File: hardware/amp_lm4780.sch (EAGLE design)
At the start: 77 parts, among them IC2 OPA2333D, Q1 MOSFET-NCHANNEL_SOT23-3, Q2 MOSFET-NCHANNEL_SOT23-3, T1 BC856, X1 2508-5, X2 uC

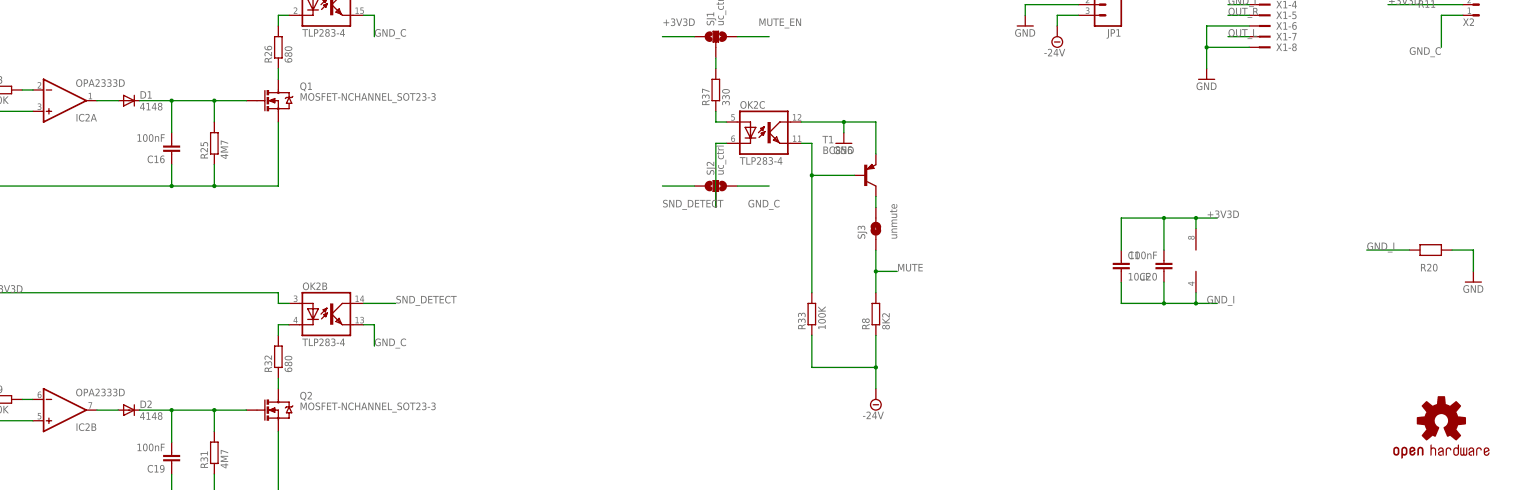
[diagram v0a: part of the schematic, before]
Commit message: fix gnd_c in amp_lm4780
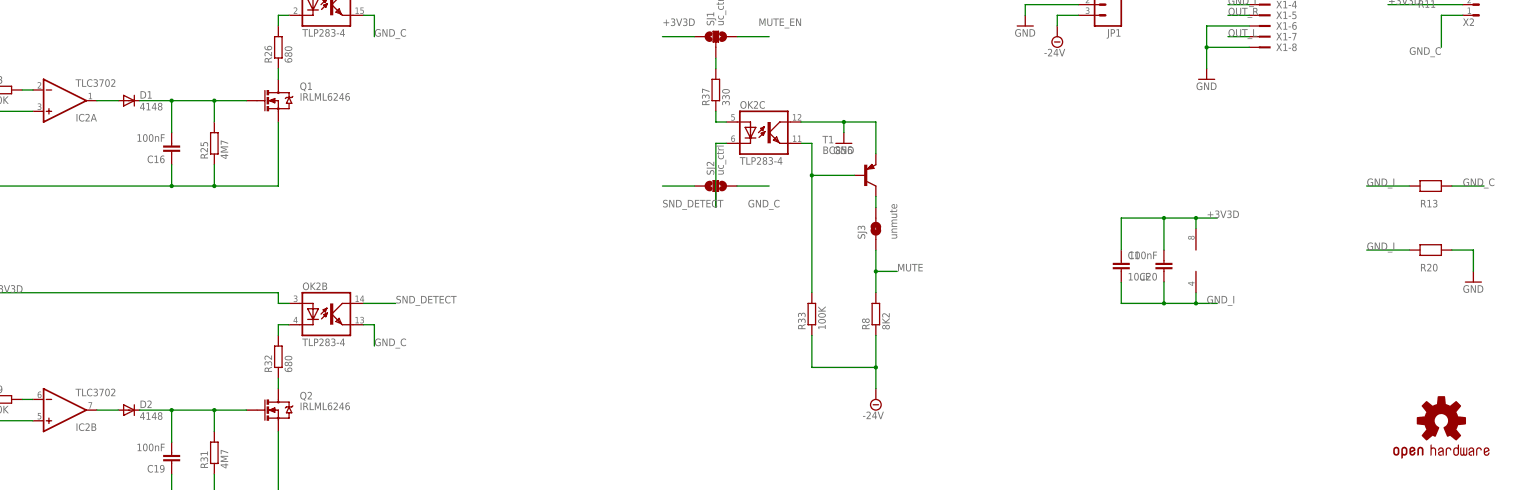
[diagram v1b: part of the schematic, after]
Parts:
- added R13: 0R_0805, Simplex-Jumpers:0R_0805
- IC2: value OPA2333D -> TLC3702
- Q1, Q2: value MOSFET-NCHANNEL_SOT23-3 -> IRLML6246
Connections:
- net N$16 renamed NONINV_IN_A
- net N$24 renamed INV_IN_A
- net N$27 renamed OUT_A
- net N$29 renamed NONINV_IN_B
- net N$32 renamed INV_IN_B
- net N$34 renamed OUTB
- net GND_C: now also R13.P$2
- net GND_I: now also R13.P$1
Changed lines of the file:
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@@
 <part name="R24" library="rcl" deviceset="R-EU_" device="R0805W" value="4M7"/>
 <part name="C15" library="rcl" deviceset="C-EU" device="C0805" value="100nF"/>
-<part name="IC2" library="linear" deviceset="OPA2333" device="D"/>
+<part name="IC2" library="linear" deviceset="OPA2333" device="D" value="TLC3702"/>
 <part name="C16" library="rcl" deviceset="C-EU" device="C0805" value="100nF"/>
 <part name="R25" library="rcl" deviceset="R-EU_" device="R0805W" value="4M7"/>
-<part name="Q1" library="Simplex-DiscreteSemi" deviceset="MOSFET-NCHANNEL" device="_SOT23-3"/>
+<part name="Q1" library="Simplex-DiscreteSemi" deviceset="MOSFET-NCHANNEL" device="_SOT23-3" value="IRLML6246"/>
 <part name="D1" library="diode" deviceset="CGRM400*-G" device="" technology="1" value="4148"/>
 <part name="R26" library="rcl" deviceset="R-EU_" device="R0805W" value="680"/>
@@
 <part name="C19" library="rcl" deviceset="C-EU" device="C0805" value="100nF"/>
 <part name="R31" library="rcl" deviceset="R-EU_" device="R0805W" value="4M7"/>
-<part name="Q2" library="Simplex-DiscreteSemi" deviceset="MOSFET-NCHANNEL" device="_SOT23-3"/>
+<part name="Q2" library="Simplex-DiscreteSemi" deviceset="MOSFET-NCHANNEL" device="_SOT23-3" value="IRLML6246"/>
 <part name="D2" library="diode" deviceset="CGRM400*-G" device="" technology="1" value="4148"/>
 <part name="R32" library="rcl" deviceset="R-EU_" device="R0805W" value="680"/>
@@
 <part name="R5" library="rcl" deviceset="R-EU_" device="R0805W" value="?K"/>
 <part name="R7" library="rcl" deviceset="R-EU_" device="R0805W" value="?K"/>
+<part name="R13" library="Simplex-Jumpers" deviceset="0R" device="_0805"/>
 </parts>
 <sheets>
@@
 <instance part="R5" gate="G$1" x="30.48" y="116.84" rot="R180"/>
 <instance part="R7" gate="G$1" x="33.02" y="43.18" rot="R180"/>
+<instance part="R13" gate="G$1" x="429.26" y="88.9"/>
 </instances>
 <busses>
@@
 <wire x1="236.22" y1="205.74" x2="236.22" y2="203.2" width="0.1524" layer="91"/>
 </segment>
-</net>
-<net name="N$16" class="0">
+<segment>
+<pinref part="R13" gate="G$1" pin="P$1"/>
+<wire x1="424.18" y1="88.9" x2="414.02" y2="88.9" width="0.1524" layer="91"/>
+<label x="414.02" y="88.9" size="1.778" layer="95"/>
+</segment>
+</net>
+<net name="NONINV_IN_A" class="0">
 <segment>
 <pinref part="C14" gate="G$1" pin="1"/>
@@
 </segment>
 </net>
-<net name="N$24" class="0">
+<net name="INV_IN_A" class="0">
 <segment>
 <pinref part="R23" gate="G$1" pin="2"/>
@@
 </segment>
 </net>
-<net name="N$27" class="0">
+<net name="OUT_A" class="0">
 <segment>
 <pinref part="IC2" gate="A" pin="OUT"/>
@@
 </segment>
 </net>
-<net name="N$29" class="0">
+<net name="NONINV_IN_B" class="0">
 <segment>
 <pinref part="C17" gate="G$1" pin="1"/>
@@
 </segment>
 </net>
-<net name="N$32" class="0">
+<net name="INV_IN_B" class="0">
 <segment>
 <pinref part="R29" gate="G$1" pin="2"/>
@@
 </segment>
 </net>
-<net name="N$34" class="0">
+<net name="OUTB" class="0">
 <segment>
 <wire x1="111.76" y1="35.56" x2="116.84" y2="35.56" width="0.1524" layer="91"/>
@@
 <label x="266.7" y="83.82" size="1.778" layer="95"/>
 </segment>
-</net>
+<segment>
+<pinref part="R13" gate="G$1" pin="P$2"/>
+<wire x1="434.34" y1="88.9" x2="441.96" y2="88.9" width="0.1524" layer="91"/>
+<label x="436.88" y="88.9" size="1.778" layer="95"/>
+</segment>
+</net>

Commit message: add buffer to snd detect circuit
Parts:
- added C27, C28, C29: 100nF, rcl:C-EUC0805
- added D3, D4, D5, D6: BZM55C3V3, diode:DIODE-MICROMELF-W
- added IC1: OPA2333, linear:OPA2333D
- added R14, R34: 4K7, rcl:R-EU_R0805W
- added R15, R41: 10K, rcl:R-EU_R0805W
- added R17, R40: 47K, rcl:R-EU_R0805W
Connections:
- new net N$11: D3.C, D4.A, IC1A.-IN, R15.1, R17.2
- new net N$12: IC1B.+IN, R34.2
- new net N$13: IC1B.OUT, R40.1, R7.2
- new net N$15: D5.C, D6.A, IC1B.-IN, R40.2, R41.1
- new net N$16: C29.1, SJ5.1
- new net N$17: C29.2, R41.2
- new net N$18: C28.2, R15.2
- new net N$19: C28.1, SJ6.1
- net +3V3D: now also C27.2, D4.C, D6.C, IC1P.V+
- net GND_I: now also C27.1, D3.A, D5.A, IC1P.V-, R14.1, R34.1
- net N$5: now also IC1A.+IN, R14.2; no longer R7.2, SJ5.1
- net N$7: now also IC1A.OUT, R17.1; no longer SJ6.1
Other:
- moved on the sheet: C1, C14, C15, C16, C17, C18, C19, D1, D2, IC2A, IC2B, OK2A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

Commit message: redesign snd_detect circuit layout
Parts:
- removed D4, D6: BZM55C3V3, diode:DIODE-MICROMELF-W
- removed R15, R41: 10K, rcl:R-EU_R0805W
- added C30, C31: 1nF, rcl:C-EUC0805
- added C32, C33: 1uF, rcl:C-EUC0805
- added C34: 10uF, rcl:C-EUC1206K
- added D7, D8: BZM55C3V3, diode:DIODE-MICROMELF-W
- added R42, R43: DNP 100K, rcl:R-EU_R0805W
- added R44, R45: DNP, rcl:R-EU_R0805W
- added R46, R47: 1K, rcl:R-EU_R0805W
- added R48, R49: 100K, rcl:R-EU_R0805W
- C28, C29: value 100nF -> 1uF
- R14, R34: value 4K7 -> 10K
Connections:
- removed net N$11: D3.C, D4.A, IC1A.-IN, R15.1, R17.2
- removed net N$15: D5.C, D6.A, IC1B.-IN, R40.2, R41.1
- new net N$20: C32.2, R14.1
- new net N$24: C29.2, R45.1, R46.1
- new net N$27: C31.2, D5.C, D8.C, IC1A.+IN, R46.2, R48.2
- new net N$29: C33.2, R34.1
- net +3V3D: now also C34.1; no longer D4.C, D6.C
- net GND_I: now also C30.1, C31.1, C32.1, C33.1, C34.2, D7.A, D8.A, R42.2, R43.2, R44.2, R45.2, R48.1, R49.1; no longer R14.1, R34.1
- net IN_L: now also SJ5.2; no longer SJ6.2
- net IN_R: now also SJ6.2; no longer SJ5.2
- net N$12: now also IC1A.-IN, R40.2; no longer IC1B.+IN
- net N$13: now also IC1A.OUT; no longer IC1B.OUT
- net N$16: now also C28.1, R42.1, SJ6.1; no longer C29.1, SJ5.1
- net N$17: now also C30.2, D3.C, D7.C, IC1B.+IN, R47.2, R49.2; no longer C29.2, R41.2
- net N$18: now also R44.1, R47.1; no longer R15.2
- net N$19: now also C29.1, R43.1, SJ5.1; no longer C28.1, SJ6.1
- net N$5: now also IC1B.-IN, R17.2; no longer IC1A.+IN
- net N$7: now also IC1B.OUT; no longer IC1A.OUT
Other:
- moved on the sheet: C15, C18, C28, C29, IC1A, IC1B, R14, R24, R30, R34, R5, R7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

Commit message: snd_detect cleanup
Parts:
- removed C32, C33: 1uF, rcl:C-EUC0805
- removed D7, D8: BZM55C3V3, diode:DIODE-MICROMELF-W
- removed R42, R43: DNP 100K, rcl:R-EU_R0805W
- removed R44, R45: DNP, rcl:R-EU_R0805W
- added D4, D6: 4148, diode:CGRM4001-G
- D3, D5: value BZM55C3V3 -> 4148; device diode:DIODE-MICROMELF-W -> diode:CGRM4001-G
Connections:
- removed net N$20: C32.2, R14.1
- removed net N$29: C33.2, R34.1
- net GND_I: now also D3.C, D4.C, D6.A, R14.1, R34.1; no longer C32.1, C33.1, D3.A, D7.A, D8.A, R42.2, R43.2, R44.2, R45.2
- net N$16: no longer R42.1
- net N$17: now also D3.A, D5.C; no longer D3.C, D7.C
- net N$18: no longer R44.1
- net N$19: no longer R43.1
- net N$24: no longer R45.1
- net N$27: now also D4.A, D6.C; no longer D5.C, D8.C
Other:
- moved on the sheet: D3, D5, R14, R34

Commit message: snd_detect revisited
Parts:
- added C32, C33: 100nF, rcl:C-EUC0805
- C14, C17: value 100nF -> 470nF
- D1, D2, D4, D6: value 4148 -> 1N4148
- R22, R28: value 150K -> 47K
- R23, R29: value 100K -> 47K
- R3, R6: value ?K -> 47K
- R5, R7: value ?K -> 1K
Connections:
- net OUTB renamed N$29
- net OUT_A renamed N$15
- removed net GND_I: C1.2, C14.2, C16.1, C17.2, C19.1, C20.1, C22.2, C23.2, C27.1, C30.1, C31.1, C34.2, D3.C, D4.C, D5.A, D6.A, IC1P.V-, IC2P.V-, Q1.S, Q2.S, R13.P$1, R14.1, R18.E, R20.P$1, R21.2, R25.1, R27.2, R3.1, R31.1, R34.1, R35.1, R36.E, R38.1, R48.1, R49.1, R6.1, X1-2.KL, X1-4.KL
- removed net INV_IN_A: IC2A.-IN, R23.2
- removed net INV_IN_B: IC2B.-IN, R29.2
- removed net NONINV_IN_A: C14.1, IC2A.+IN, R21.1, R22.1
- removed net NONINV_IN_B: C17.1, IC2B.+IN, R27.1, R28.1
- new net GNDI: C1.2, C14.2, C16.1, C17.2, C19.1, C20.1, C22.2, C23.2, C27.1, C30.1, C31.1, C32.1, C33.1, C34.2, D3.C, D4.C, D5.A, D6.A, IC1P.V-, IC2P.V-, Q1.S, Q2.S, R13.P$1, R14.1, R18.E, R20.P$1, R21.2, R25.1, R27.2, R3.1, R31.1, R34.1, R35.1, R36.E, R38.1, R48.1, R49.1, R6.1, X1-2.KL, X1-4.KL
- new net N$11: C15.2, R21.1, R22.1, R23.1
- new net N$20: IC2A.+IN, R23.2
- new net N$32: C18.2, R27.1, R28.1, R29.1
- new net N$34: IC2B.+IN, R29.2
- net N$13: now also R5.2; no longer R7.2
- net N$23: now also C14.1, IC2A.-IN; no longer C15.2, R23.1
- net N$26: now also C32.2
- net N$31: now also C17.1, IC2B.-IN; no longer C18.2, R29.1
- net N$33: now also C33.2
- net N$7: now also R7.2; no longer R5.2
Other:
- moved on the sheet: C10, C12, C14, C15, C16, C17, C18, C19, C2, C23, C24, C25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

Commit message: cleanup
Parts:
- C32, C33: value 100nF -> 1nF
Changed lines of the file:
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@@
 <part name="GNDI24" library="supply1" deviceset="GNDI" device=""/>
 <part name="GNDI25" library="supply1" deviceset="GNDI" device=""/>
-<part name="C32" library="rcl" deviceset="C-EU" device="C0805" value="100nF"/>
-<part name="C33" library="rcl" deviceset="C-EU" device="C0805" value="100nF"/>
+<part name="C32" library="rcl" deviceset="C-EU" device="C0805" value="1nF"/>
+<part name="C33" library="rcl" deviceset="C-EU" device="C0805" value="1nF"/>
 <part name="GNDI26" library="supply1" deviceset="GNDI" device=""/>
 <part name="GNDI27" library="supply1" deviceset="GNDI" device=""/>

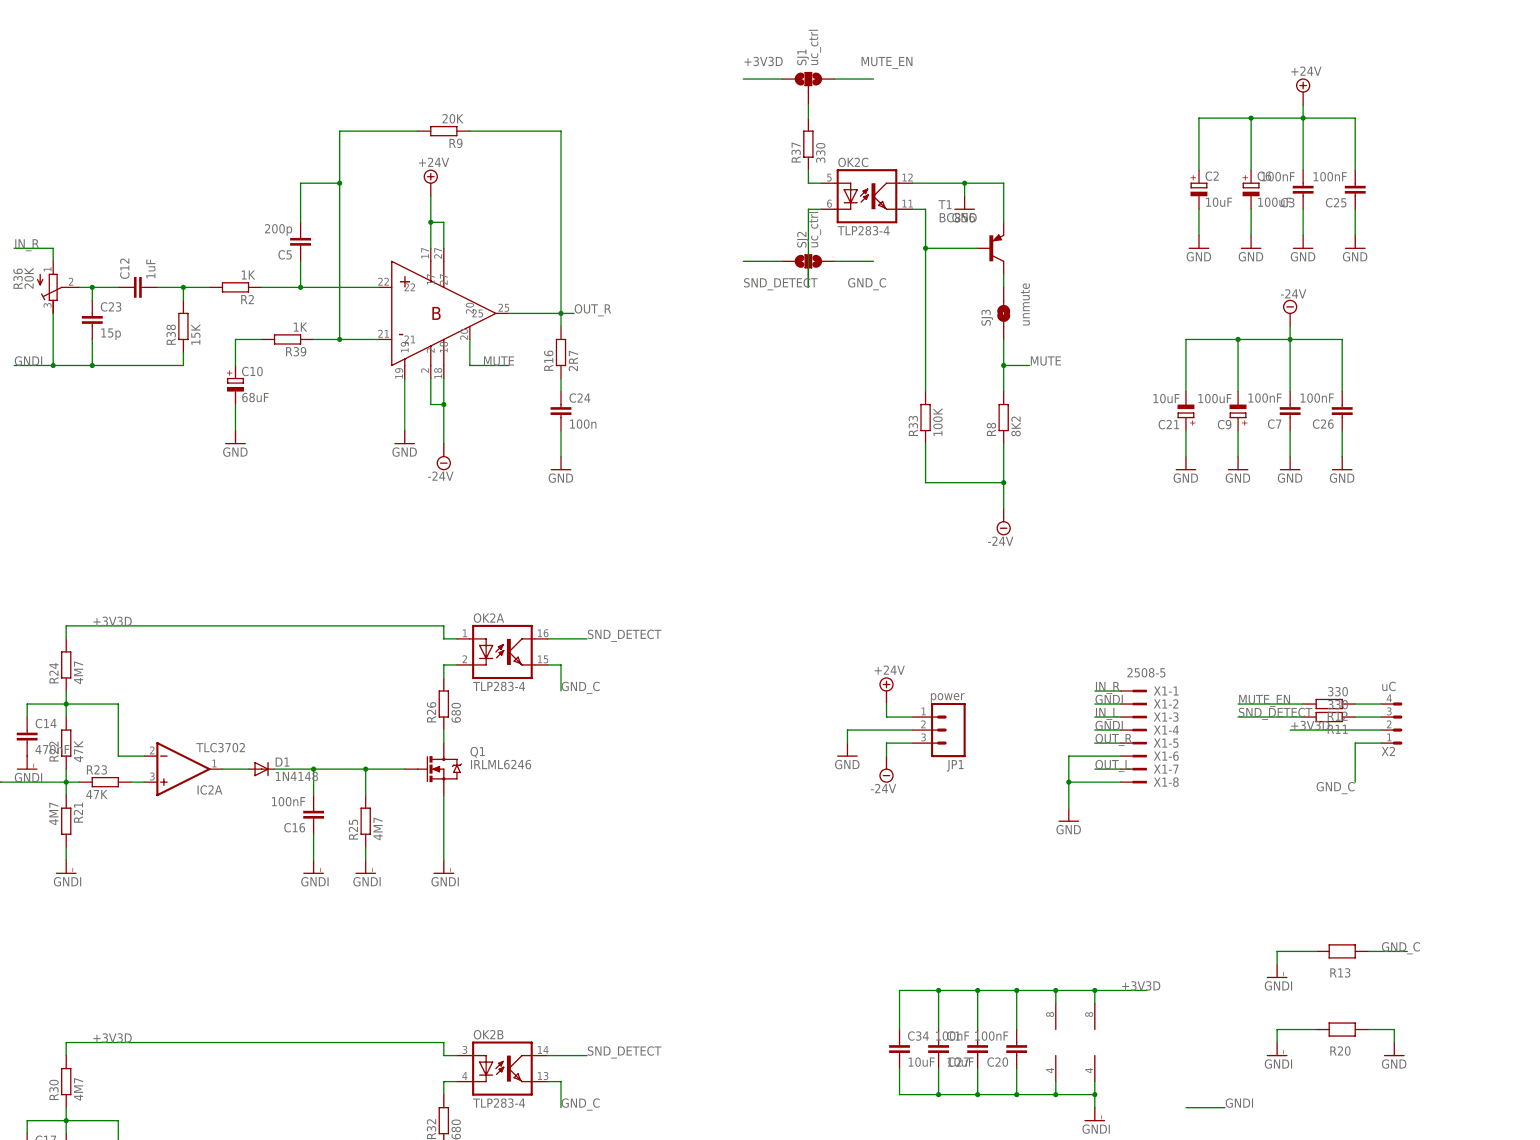
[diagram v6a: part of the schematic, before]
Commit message: add debug window into ncurses cli
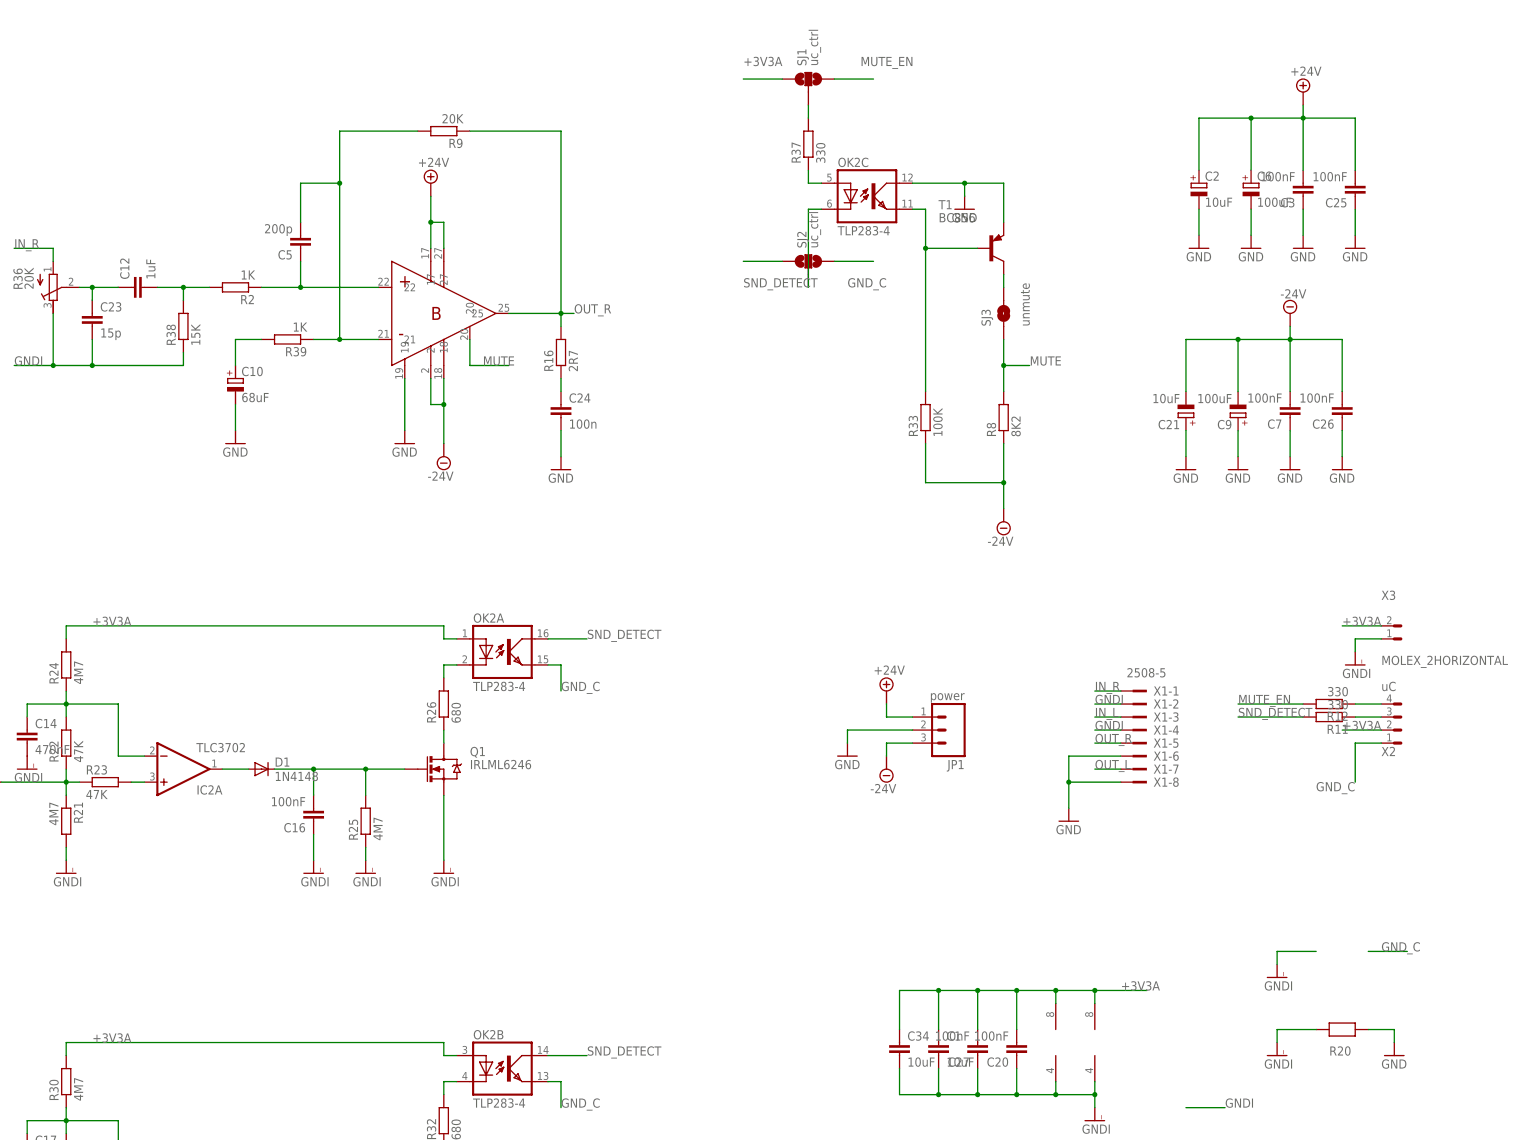
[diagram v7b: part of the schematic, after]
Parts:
- removed R13: 0R_0805, Simplex-Jumpers:0R_0805
- added X3: MOLEX_2HORIZONTAL, Simplex-Connectors:MOLEX_2HORIZONTAL
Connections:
- removed net +3V3D: C1.1, C20.2, C27.2, C34.1, IC1P.V+, IC2P.V+, OK2A.A, OK2B.A, R24.2, R30.2, SJ1.1, X2.3
- new net +3V3A: C1.1, C20.2, C27.2, C34.1, IC1P.V+, IC2P.V+, OK2A.A, OK2B.A, R24.2, R30.2, SJ1.1, X2.3, X3.1
- net GNDI: now also X3.2; no longer R13.P$1
- net GND_C: no longer R13.P$2
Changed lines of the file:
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@@
 <part name="R5" library="rcl" deviceset="R-EU_" device="R0805W" value="1K"/>
 <part name="R7" library="rcl" deviceset="R-EU_" device="R0805W" value="1K"/>
-<part name="R13" library="Simplex-Jumpers" deviceset="0R" device="_0805"/>
 <part name="IC1" library="linear" deviceset="OPA2333" device="D" value="OPA2333"/>
 <part name="R14" library="rcl" deviceset="R-EU_" device="R0805W" value="10K"/>
@@
 <part name="GNDI26" library="supply1" deviceset="GNDI" device=""/>
 <part name="GNDI27" library="supply1" deviceset="GNDI" device=""/>
+<part name="X3" library="Simplex-Connectors" deviceset="MOLEX_2" device="HORIZONTAL"/>
+<part name="GNDI28" library="supply1" deviceset="GNDI" device=""/>
 </parts>
 <sheets>
@@
 <instance part="R5" gate="G$1" x="137.16" y="121.92" rot="R180"/>
 <instance part="R7" gate="G$1" x="137.16" y="40.64" rot="R180"/>
-<instance part="R13" gate="G$1" x="429.26" y="88.9"/>
 <instance part="IC1" gate="A" x="116.84" y="121.92" rot="MR180"/>
 <instance part="IC1" gate="B" x="116.84" y="40.64" rot="MR180"/>
@@
 <instance part="GNDI26" gate="G$1" x="154.94" y="104.14"/>
 <instance part="GNDI27" gate="G$1" x="154.94" y="22.86"/>
+<instance part="X3" gate="G$1" x="439.42" y="152.4"/>
+<instance part="GNDI28" gate="G$1" x="431.8" y="144.78"/>
 </instances>
 <busses>
@@
 </segment>
 <segment>
-<pinref part="R13" gate="G$1" pin="P$2"/>
 <wire x1="434.34" y1="88.9" x2="441.96" y2="88.9" width="0.1524" layer="91"/>
 <label x="436.88" y="88.9" size="1.778" layer="95"/>
@@
 </segment>
 </net>
-<net name="+3V3D" class="0">
+<net name="+3V3A" class="0">
 <segment>
 <label x="185.42" y="152.4" size="1.778" layer="95"/>
@@
 <wire x1="180.34" y1="71.12" x2="254" y2="71.12" width="0.1524" layer="91"/>
 <pinref part="OK2" gate="B" pin="A"/>
-</segment>
-<segment>
-<label x="419.1" y="132.08" size="1.778" layer="95"/>
-<wire x1="436.88" y1="132.08" x2="419.1" y2="132.08" width="0.1524" layer="91"/>
-<pinref part="X2" gate="G$1" pin="3"/>
 </segment>
 <segment>
@@
 <junction x="350.52" y="81.28"/>
 </segment>
+<segment>
+<pinref part="X3" gate="G$1" pin="1"/>
+<wire x1="436.88" y1="152.4" x2="429.26" y2="152.4" width="0.1524" layer="91"/>
+<label x="429.26" y="152.4" size="1.778" layer="95"/>
+</segment>
+<segment>
+<pinref part="X2" gate="G$1" pin="3"/>
+<wire x1="436.88" y1="132.08" x2="429.26" y2="132.08" width="0.1524" layer="91"/>
+<label x="429.26" y="132.08" size="1.778" layer="95"/>
+</segment>
 </net>
 <net name="N$21" class="0">
@@
 </segment>
 <segment>
-<pinref part="R13" gate="G$1" pin="P$1"/>
 <pinref part="GNDI24" gate="G$1" pin="GNDI"/>
 <wire x1="424.18" y1="88.9" x2="416.56" y2="88.9" width="0.1524" layer="91"/>
@@
 <wire x1="154.94" y1="109.22" x2="154.94" y2="106.68" width="0.1524" layer="91"/>
 </segment>
-</net>
+<segment>
+<pinref part="X3" gate="G$1" pin="2"/>
+<pinref part="GNDI28" gate="G$1" pin="GNDI"/>
+<wire x1="436.88" y1="149.86" x2="431.8" y2="149.86" width="0.1524" layer="91"/>
+<wire x1="431.8" y1="149.86" x2="431.8" y2="147.32" width="0.1524" layer="91"/>
+</segment>
+</net>
